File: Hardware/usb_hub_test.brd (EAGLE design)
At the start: 77.5 x 32.6 mm, 99 parts, among them CN1 54819-0519, CN2 TSW-120-08-L-S-RA, CN4 1-1734530-1, IC1 FT230XQ, IC2 TUSB2046BIRHBT, IC3 MAX3375, IC4 PIC24FJ128GA202-I/MM, IC5 FT230XQ, IC7 MAX3375

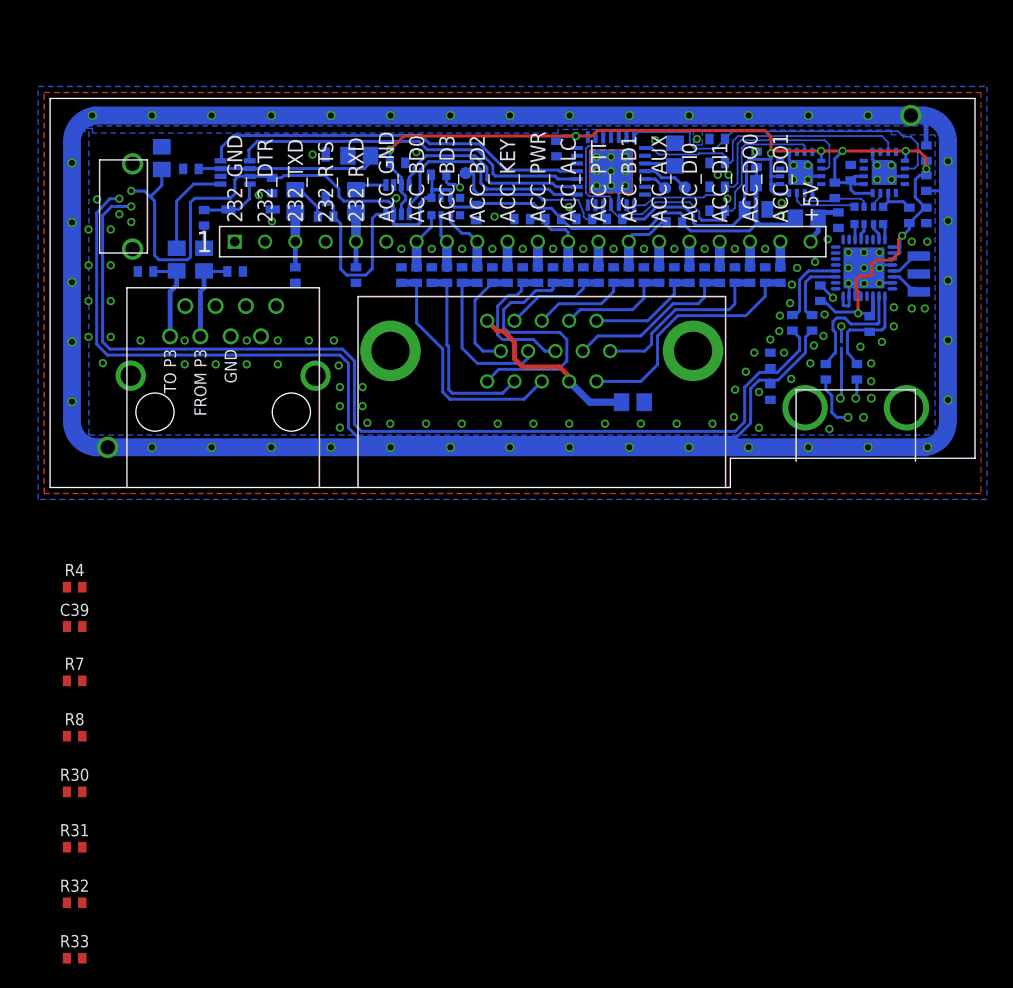
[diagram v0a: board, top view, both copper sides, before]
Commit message: Implementing Board changes from v1
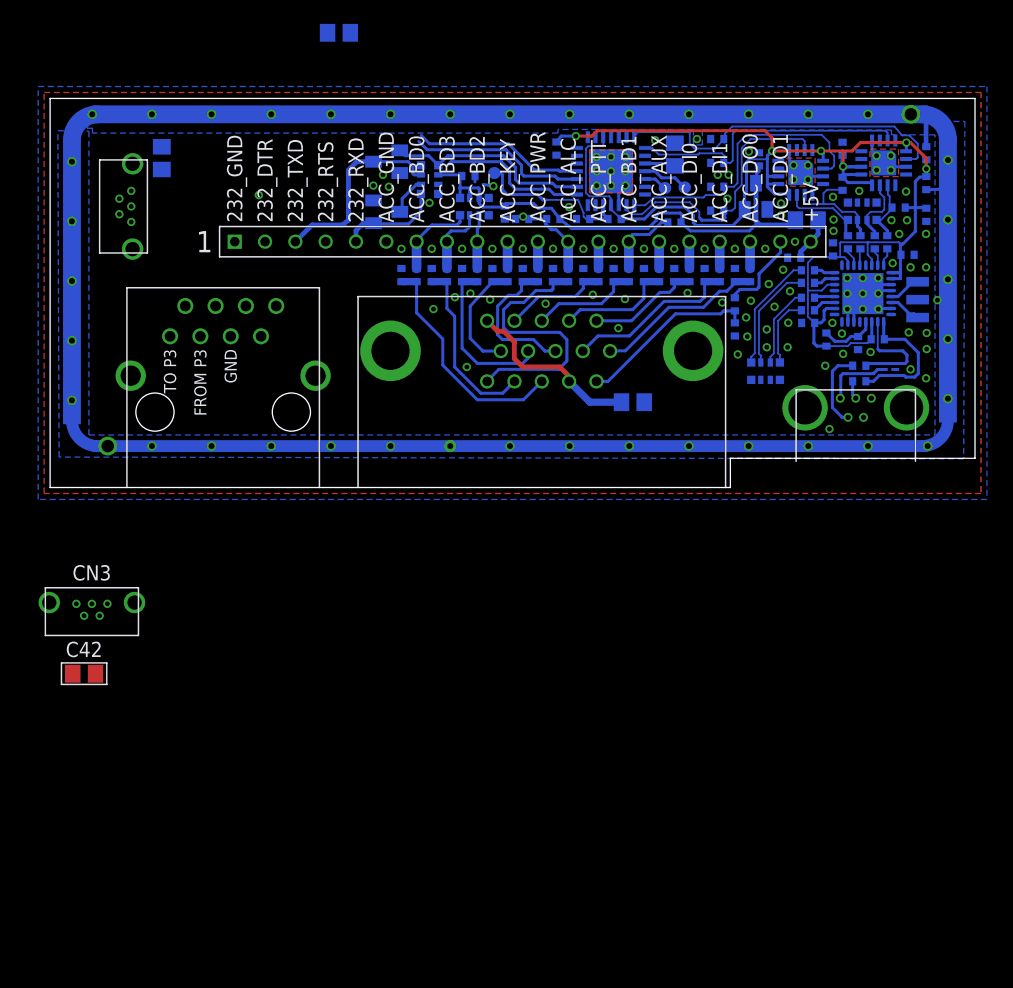
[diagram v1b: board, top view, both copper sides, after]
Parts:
- removed C1, C35, C37: 100nF, rcl:C0402
- removed C27, C28, C33, C34: 1nF, rcl:C0402
- removed D2, D3: BZT52C4V7-7-F, adafruit:SOD-123
- removed IC3, IC7: MAX3375, m0wut:SOT23-8L
- removed L2, L3, L5, L6: 100uH, m0wut:R0805
- removed R12, R3: 220, rcl:R0402
- removed R5, R6: 15k, rcl:R0402
- added C40, C41: 100nF, rcl:C0402
- added C42: 10uF, rcl:C0805
- added CN3: (no value), m0wut:USB_WURTH_3145-30-1-A
- added Q1, Q2: (no value), adafruit:SOT23
- added RN3: 27, m0wut:R_BOURNS_CAY16-J4
- added RN4: (no value), m0wut:R_BOURNS_CAY16-J4
- R15, R16: value 27 -> (none)
- R30, R31, R32, R33, R7, R8: value 15k -> (none)
- RN2: value (none) -> 27
- moved R33 88.3 mm to (66.8, 20.6), flipped to the bottom, turned to 90 degrees
- moved R32 86.0 mm to (67.9, 20.6), flipped to the bottom, turned to 90 degrees
- moved R31 84.1 mm to (69.1, 20.6), flipped to the bottom, turned to 90 degrees
- moved R30 82.2 mm to (70.2, 20.6), flipped to the bottom, turned to 90 degrees
- moved R8 71.6 mm to (63.5, 15.9), flipped to the bottom, turned to 180 degrees
- moved C39 69.8 mm to (67.7, 12.1), flipped to the bottom, turned to 270 degrees
- moved R7 68.8 mm to (63.5, 14.8), flipped to the bottom, turned to 180 degrees
- moved R4 66.3 mm to (65.0, 12.4), flipped to the bottom, turned to 90 degrees
- moved RN2 15.7 mm to (60.0, 9.75)
- moved C8 10.4 mm to (24.2, 38.1)
- moved C21 5.21 mm to (57.4, 13.2), turned to 270 degrees
- moved C26 4.86 mm to (62.4, 19.2), turned to 0 degrees
- moved R16 4.59 mm to (63.5, 18.2), turned to 180 degrees
- moved R26 4.53 mm to (57.4, 15.3)
- moved D1 4.52 mm to (70.3, 9.89), turned to 270 degrees
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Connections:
- removed net N$188: IC3.1, L2.1
- removed net N$189: D2.C, IC3.8, R12.1
- removed net N$4: D3.C, IC7.8, R3.1
- removed net N$5: IC7.1, L5.1
- removed net N$6: L3.1, R12.2
- removed net N$7: L6.1, R3.2
- removed net P3_RXD: C27.1, L5.2, U$1.1
- removed net P3_TXD: C28.1, L6.2, U$1.3
- new net N$18: CN3.2, R15.1, RN2.3A
- new net N$19: CN3.3, R16.1, RN2.4A
- net +3V3: now also C40.1, C41.1, RN4.2A; no longer C1.1, C35.1, IC3.3, IC3.6, IC7.3, IC7.6
- net +5V: now also C42.1, CN3.1, RN4.3A; no longer C37.1, IC3.7, IC7.7
- net 232_RXD: now also Q2.1, RN4.1; no longer C33.1, L2.2
- net 232_TXD: now also Q1.3, RN4.3; no longer C34.1, L3.2
- net DM1: now also R7.1, RN2.1A; no longer R15.1, R5.2
- net DM3: now also R33.2, RN3.1A; no longer R30.2, RN2.4A
- net DM4: now also R31.2, RN3.3A; no longer R32.2, RN2.2A
- net DP1: now also R8.1, RN2.2A; no longer R16.1, R6.2
- net DP3: now also R32.2, RN3.2A; no longer R31.2, RN2.3A
- net DP4: now also R30.2, RN3.4A; no longer R33.2, RN2.1A
- net GND: now also C40.2, C41.2, C42.2, CN3.4, CN3.5, CN3.P$1, CN3.P$2, IC1.P$1, IC1.P$2, IC1.P$3, IC1.P$4, IC5.P$1, IC5.P$2, IC5.P$3, IC5.P$4, Q1.2, Q2.2, RN2.1, RN2.2, RN2.3, RN2.4, RN3.1, RN3.2, RN3.3, RN3.4, RN4.1A, RN4.4; no longer C1.2, C27.2, C28.2, C33.2, C34.2, C35.2, C37.2, D2.A, D3.A, IC3.2, IC7.2, R30.1, R31.1, R32.1, R33.1, R5.1, R6.1, R7.1, R8.1
- net N$1: now also R31.1; no longer RN2.2
- net N$11: now also R15.2; no longer R8.2
- net N$12: now also R7.2; no longer R15.2
- net N$13: now also R8.2; no longer R16.2
- net N$14: now also R16.2; no longer R7.2
- net N$16: now also R32.1; no longer RN2.3
- net N$17: now also R33.1; no longer RN2.4
- net N$3: now also R30.1; no longer RN2.1
- net UART_FROM_K3: now also Q2.3, RN4.2; no longer IC3.5
- net UART_FROM_P3: no longer IC7.5
- net UART_TO_K3: now also Q1.1, RN4.4A; no longer IC3.4
- net UART_TO_P3: no longer IC7.4
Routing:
- net DM1: track 86.3 -> 5.86 mm
- net DP1: track 84.7 -> 6.94 mm
- net +5V: track 86.7 -> 42.5 mm
- net UART_TO_P3: track 32.6 -> 14.3 mm
- net +3V3: track 150.5 -> 133.6 mm, vias 9 -> 6
- net UART_FROM_P3: track 30.4 -> 15.0 mm
- net N$189: track 15.3 -> 0.00 mm
- net 232_TXD: track 4.60 -> 16.5 mm
- net N$19: track 0.00 -> 9.85 mm
- net N$18: track 0.00 -> 8.91 mm
- net N$5: track 8.22 -> 0.00 mm
- net P3_RXD: track 7.68 -> 0.00 mm
- net P3_TXD: track 7.58 -> 0.00 mm
- net DIGO1_X: track 20.9 -> 15.0 mm
- net N$4: track 5.43 -> 0.00 mm
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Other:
- board text added: "KIO3WUT MØWUT v0.2"
- board text removed: "KIO3WUT MØWUT v0.12"

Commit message: v2 pcb ordered
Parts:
- removed CAN2: CAN_MASTECH, m0wut:CAN_MASTECH_MS737-10F
- added C1, C35, C37: 100nF, rcl:C0402
- added C27, C28, C33, C43, C44: 1nF, rcl:C0402
- added C34: 10uF, rcl:C0805
- added IC3: IC_MAX3313, m0wut:IC_UMAX10
- added L2, L3, L5, L6: (no value), m0wut:R0805
- added R3: 0R, rcl:R0402
- C42: value 10uF -> 100nF; device rcl:C0805 -> rcl:C0402
- CN3: value (none) -> 48204-0001; device m0wut:USB_WURTH_3145-30-1-A -> m0wut:CONN_USB_MOLEX_RA
- CN5: device m0wut:USB_WURTH_3145-30-1-A -> m0wut:USB_MICROB_WURTH
- L1: value 100uH -> (none)
- RN4: value (none) -> 10k
- moved C42 42.0 mm to (9.60, 25.9), flipped to the bottom, turned to 270 degrees
- moved L1 40.2 mm to (10.1, 17.8), turned to 270 degrees
- moved C8 18.7 mm to (40.7, 29.2), turned to 270 degrees
- moved C22 15.0 mm to (40.3, 7.50), turned to 180 degrees
- moved C17 13.8 mm to (45.6, 7.50), turned to 180 degrees
- moved C38 10.8 mm to (2.60, 19.2), turned to 0 degrees
- moved C16 10.4 mm to (49.1, 11.5), turned to 180 degrees
- moved C24 10.4 mm to (34.7, 10.6)
- moved C21 9.99 mm to (48.4, 8.88), turned to 180 degrees
- moved CN3 9.78 mm to (4.30, 0.00)
- moved CN5 7.23 mm to (0.00, 26.0), flipped to the bottom, turned to 90 degrees
- moved C20 5.21 mm to (34.5, 13.3), turned to 0 degrees
- moved C13 4.32 mm to (47.8, 14.0), turned to 270 degrees
- moved C23 2.95 mm to (32.6, 14.9), turned to 0 degrees
- moved R26 2.84 mm to (58.8, 17.8)
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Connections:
- removed net N$18: CN3.2, R15.1, RN2.3A
- removed net N$19: CN3.3, R16.1, RN2.4A
- new net 232_FROM_P3: C44.1, L5.2, U$1.3
- new net 232_TO_P3: C43.1, L1.2, U$1.1
- new net AGND: C12.2, C13.2, C14.2, C15.2, C16.2, C17.2, C18.2, C19.2, C20.2, C21.2, C22.2, C23.2, C24.2, C27.2, C28.2, C33.2, C43.2, C44.2, CN4.16, CN4.17, U$1.TAB, U$1.TAB1
- new net ASDF: L3.1, Q1.3, RN4.3
- new net DM2: CN5.2, R15.1, RN2.3A
- new net DP2: CN5.3, R16.1, RN2.4A
- new net N$15: C37.1, IC3.8
- new net N$4: C42.1, IC3.1, L6.2
- new net N$6: C35.1, IC3.2
- new net N$7: C35.2, IC3.9
- new net SADF: L2.1, Q2.1, RN4.2
- new net WTRE: IC3.7, L1.1
- new net Y5W4: IC3.6, L5.1
- net +3V3: now also C1.1, RN4.1A; no longer RN4.2A
- net +5V: now also C34.1, L6.1; no longer C42.1
- net 232_RXD: now also C28.1, L2.2; no longer Q2.1, RN4.1
- net 232_TXD: now also C27.1, L3.2; no longer Q1.3, RN4.3
- net ACC_COMMON: now also C33.1, R3.2; no longer L1.2
- net DM1: now also CN3.2; no longer CN5.2
- net DP1: now also CN3.3; no longer CN5.3
- net GND: now also C1.2, C34.2, C37.2, CN3.P$3, CN3.P$4, CN3.P$5, CN5.GND1, CN5.GND2, CN5.GND3, CN5.GND4, IC3.10, R3.1, RN4.2A, RN4.4A; no longer C12.2, C13.2, C14.2, C15.2, C16.2, C17.2, C18.2, C19.2, C20.2, C21.2, C22.2, C23.2, C24.2, CAN2.P$1, CAN2.P$2, CAN2.P$3, CAN2.P$4, CAN2.P$5, CAN2.P$6, CAN2.TAB@1, CAN2.TAB@10, CAN2.TAB@11, CAN2.TAB@12, CAN2.TAB@13, CAN2.TAB@14, CAN2.TAB@15, CAN2.TAB@16, CAN2.TAB@17, CAN2.TAB@18, CAN2.TAB@19, CAN2.TAB@2, CAN2.TAB@20, CAN2.TAB@21, CAN2.TAB@22, CAN2.TAB@23, CAN2.TAB@24, CAN2.TAB@25, CAN2.TAB@26, CAN2.TAB@27, CAN2.TAB@28, CAN2.TAB@29, CAN2.TAB@3, CAN2.TAB@30, CAN2.TAB@31, CAN2.TAB@32, CAN2.TAB@33, CAN2.TAB@34, CAN2.TAB@35, CAN2.TAB@36, CAN2.TAB@37, CAN2.TAB@38, CAN2.TAB@4, CAN2.TAB@5, CAN2.TAB@6, CAN2.TAB@7, CAN2.TAB@8, CAN2.TAB@9, CN3.5, CN3.P$1, CN4.16, CN4.17, CN5.P$1, CN5.P$2, L1.1, RN4.1A, RN4.4, U$1.TAB, U$1.TAB1
- net UART_FROM_K3: now also RN4.1; no longer RN4.2
- net UART_FROM_P3: now also IC3.5
- net UART_TO_K3: now also RN4.4; no longer RN4.4A
- net UART_TO_P3: now also IC3.4
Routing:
- net DP2: track 0.00 -> 93.1 mm
- net DM2: track 0.00 -> 93.0 mm
- net DM1: track 5.86 -> 82.7 mm
- net DP1: track 6.94 -> 81.0 mm
- net +5V: track 42.5 -> 95.7 mm, vias 0 -> 2
- net +3V3: track 133.6 -> 156.3 mm, vias 6 -> 7
- net UART_TO_P3: track 14.3 -> 35.3 mm
- net UART_FROM_P3: track 15.0 -> 35.0 mm
- net ASDF: track 0.00 -> 11.3 mm
- net 232_TXD: track 16.5 -> 5.37 mm
- net SADF: track 0.00 -> 10.6 mm
- net N$19: track 9.85 -> 0.00 mm
- net N$18: track 8.91 -> 0.00 mm
- net GND: track 34.8 -> 43.5 mm, vias 86 -> 161
- net 232_FROM_P3: track 0.00 -> 7.63 mm
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- added copper zone on layer 1, net AGND
- added copper zone on layer 16, net AGND
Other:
- outline, holes or cut-outs redrawn
- board text added: "KIO3W MØWUT v0.2"
- board text added: "RX"
- board text added: "TX"
- board text removed: "FROM P3"
- board text removed: "KIO3WUT MØWUT v0.2"
- board text removed: "TO P3"
